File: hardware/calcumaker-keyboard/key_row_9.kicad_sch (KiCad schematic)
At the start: 30 parts, among them SW1 MX, SW10 MX, SW2 MX, SW3 MX, SW4 MX, SW5 MX, SW6 MX, SW7 MX, SW8 MX, SW9 MX

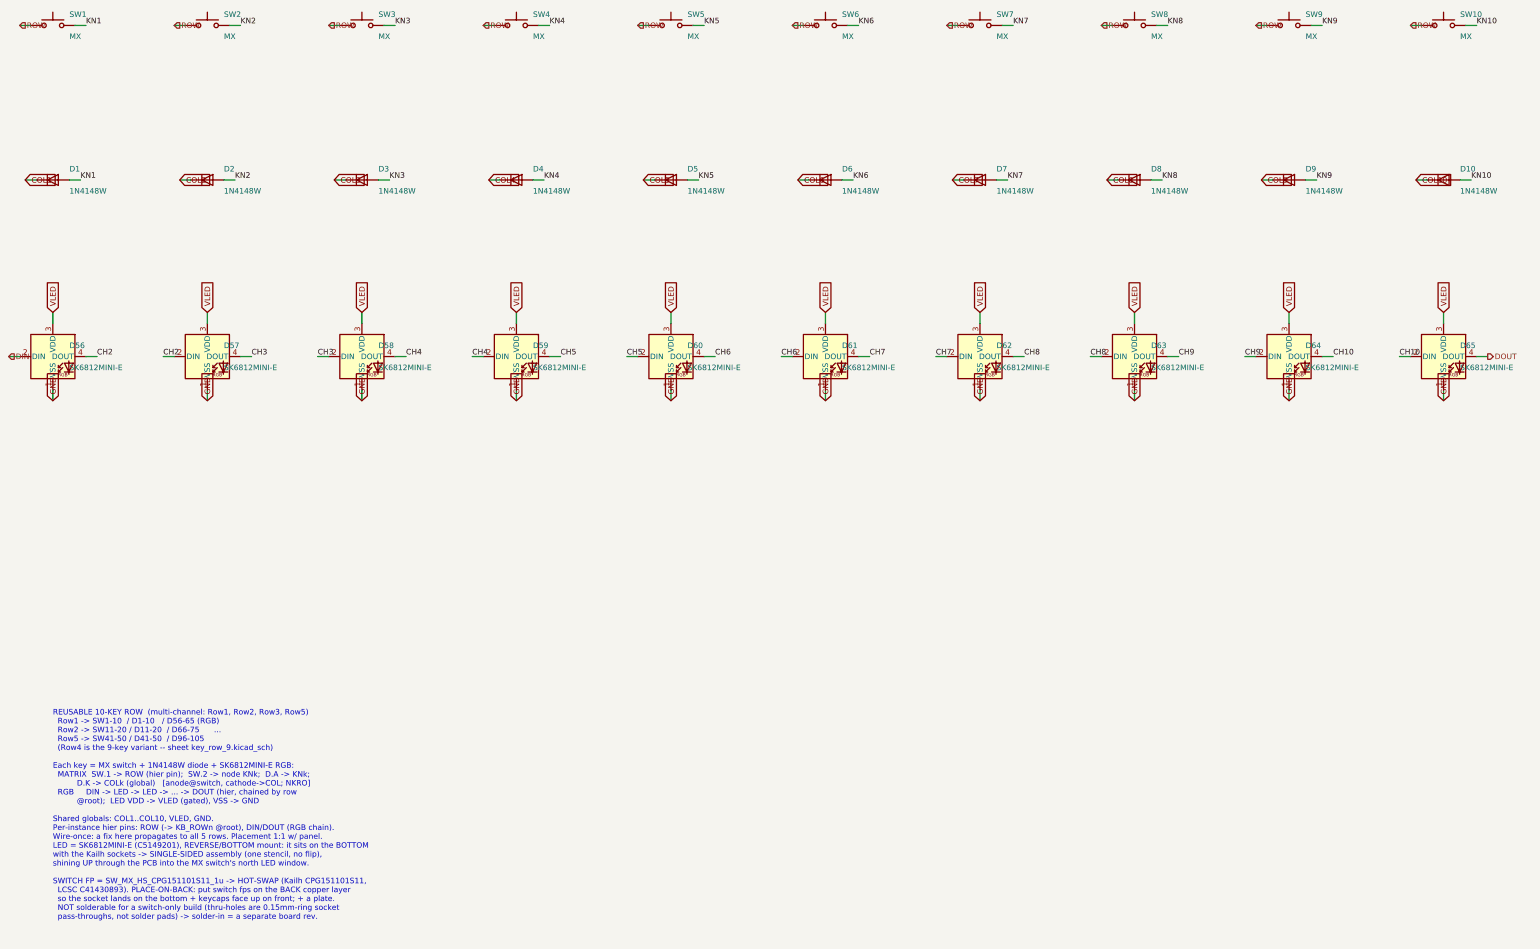
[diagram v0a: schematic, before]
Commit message: hw: regenerate keyboard for the 2U ENTER + vendor the 2U hot-swap footprint
Board files now reflect the 2U ENTER (49 keys):
- key_row.kicad_sch      -> 4 instances (Row1/2/3/5), 30 symbols
- key_row_9.kicad_sch    -> NEW, 1 instance (Row4), 27 symbols: no switch, diode
                            or RGB LED at COL6; refs keep a hole (no SW36/D36/D91)
- root note + rgb_power note updated (49 LEDs, Row4 has 9)

check-calcumaker-keyboard: 176 components (3 fewer), 176/176 footprints assigned,
no duplicate refs, structure sound. Regeneration verified safe first by running the
generator against a scratch copy: the one-off sheets (annunc/kbd_mcu/main_if)
rebuild byte-identical modulo uuids, i.e. nothing was hand-wired.

Vendored calcumaker:SW_MX_HS_CPG151101S11_2u_Vertical -- the 1u hot-swap footprint
plus the four PCB-mount 2U stabilizer NPTH holes (y = +/-11.90mm = 23.8mm spacing;
each wing a 3.05mm hole at x=-7.00 and a 4.00mm at x=+8.24), taken from stock
Button_Switch_Keyboard:SW_Cherry_MX_2.00u_Vertical_PCB and re-expressed about our
origin (already the switch centre). Courtyard grown; 2U keycap envelope on F.Fab.
KiCad 10 parses/plots it (kicad-cli fp export svg).

It is UNUSED by default: we use PLATE-mount stabilizers, which clip into the
switch plate the hot-swap sockets already require, so the PCB needs no stab holes
and ENTER just reuses MX_FP (verified: KiCad's SW_Cherry_MX_2.00u_Vertical_Plate
has the same pad/hole set as the 1u plate fp). PCB-mount would additionally force
a Row5 variant sheet, since ENTER's switch is on the shared 10-key sheet.

Place-on-back is safe: mirroring X maps the stab-hole set onto itself rotated 180,
and a 2U key is symmetric.

Co-Authored-By: Claude Opus 4.8 (1M context) <noreply@anthropic.com>
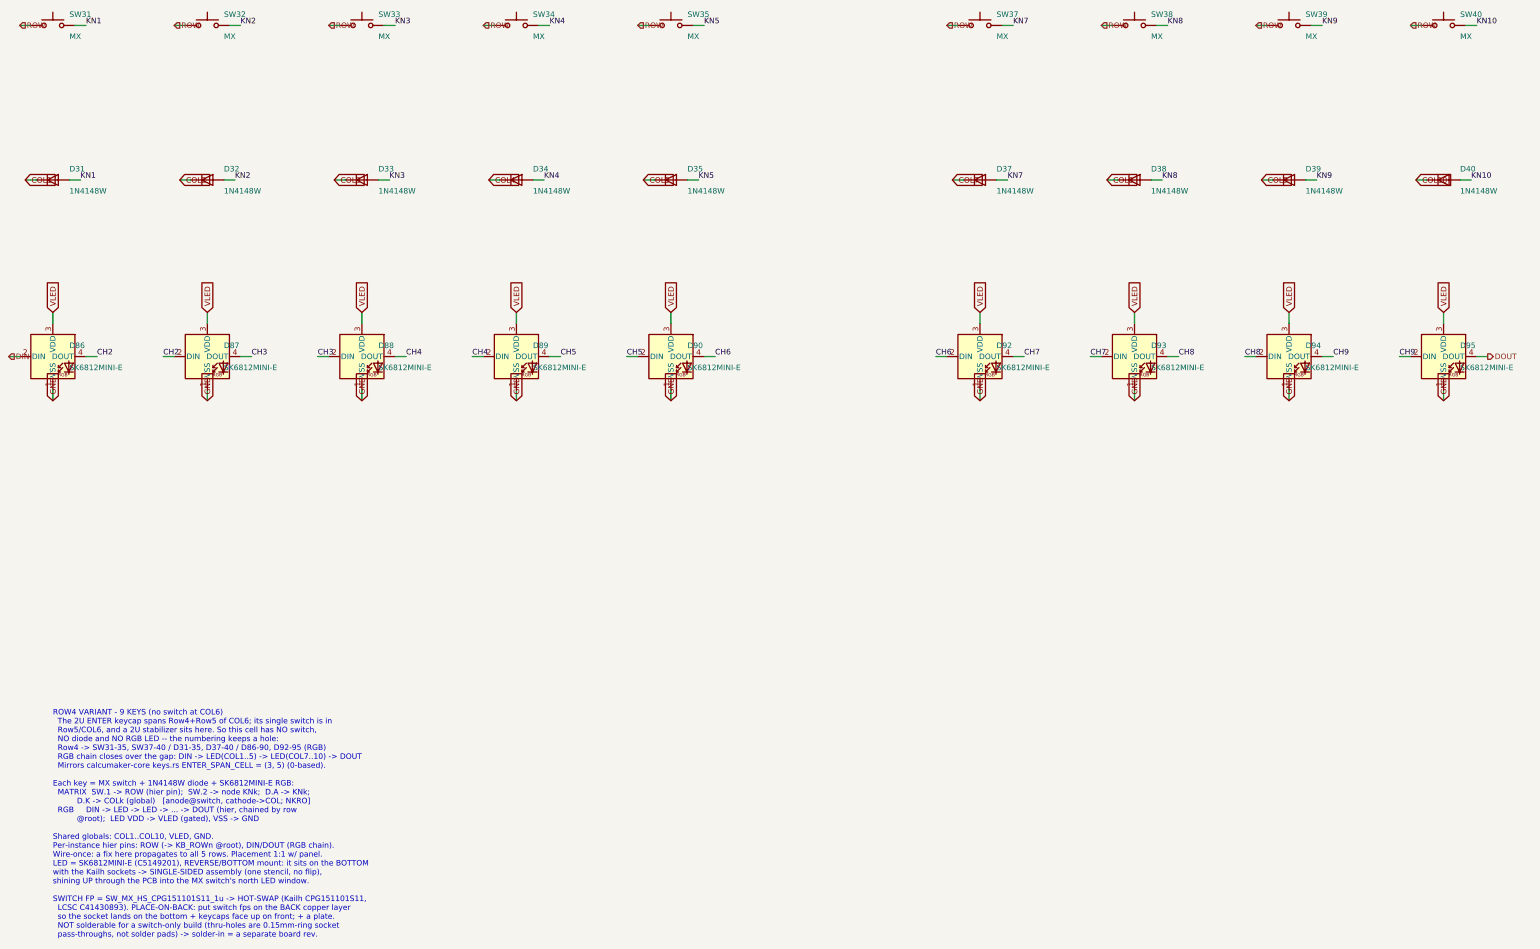
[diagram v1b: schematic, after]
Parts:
- removed D1, D10, D2, D3, D4, D5, D6, D7, D8, D9: 1N4148W, Diode_SMD:D_SOD-123, symbol Device:D
- removed D56, D57, D58, D59, D60, D61, D62, D63, D64, D65: SK6812MINI-E, LED_SMD:LED_SK6812MINI-E_3.2x2.8mm_P1.5mm_ReverseMount, symbol LED:SK6812
- removed SW1, SW10, SW2, SW3, SW4, SW5, SW6, SW7, SW8, SW9: MX, calcumaker:SW_MX_HS_CPG151101S11_1u, symbol Switch:SW_Push
- added D31, D32, D33, D34, D35, D37, D38, D39, D40: 1N4148W, Diode_SMD:D_SOD-123, symbol Device:D
- added D86, D87, D88, D89, D90, D92, D93, D94, D95: SK6812MINI-E, LED_SMD:LED_SK6812MINI-E_3.2x2.8mm_P1.5mm_ReverseMount, symbol LED:SK6812
- added SW31, SW32, SW33, SW34, SW35, SW37, SW38, SW39, SW40: MX, calcumaker:SW_MX_HS_CPG151101S11_1u, symbol Switch:SW_Push
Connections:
- net CH2: now also D86.4 (DOUT), D87.2 (DIN)
- net CH3: now also D87.4 (DOUT), D88.2 (DIN)
- net CH4: now also D88.4 (DOUT), D89.2 (DIN)
- net CH5: now also D89.4 (DOUT), D90.2 (DIN)
- net CH6: now also D90.4 (DOUT), D92.2 (DIN)
- net CH7: now also D92.4 (DOUT), D93.2 (DIN)
- net CH8: now also D93.4 (DOUT), D94.2 (DIN)
- net CH9: now also D94.4 (DOUT), D95.2 (DIN)
- net COL1: now also D31.1 (K)
- net COL10: now also D40.1 (K)
- net COL2: now also D32.1 (K)
- net COL3: now also D33.1 (K)
- net COL4: now also D34.1 (K)
- net COL5: now also D35.1 (K)
- net COL7: now also D37.1 (K)
- net COL8: now also D38.1 (K)
- net COL9: now also D39.1 (K)
- net DIN: now also D86.2 (DIN)
- net DOUT: now also D95.4 (DOUT)
- net GND: now also D86.1 (VSS), D87.1 (VSS), D88.1 (VSS), D89.1 (VSS), D90.1 (VSS), D92.1 (VSS), D93.1 (VSS), D94.1 (VSS), D95.1 (VSS)
- net KN1: now also D31.2 (A), SW31.2
- net KN10: now also D40.2 (A), SW40.2
- net KN2: now also D32.2 (A), SW32.2
- net KN3: now also D33.2 (A), SW33.2
- net KN4: now also D34.2 (A), SW34.2
- net KN5: now also D35.2 (A), SW35.2
- net KN7: now also D37.2 (A), SW37.2
- net KN8: now also D38.2 (A), SW38.2
- net KN9: now also D39.2 (A), SW39.2
- net ROW: now also SW31.1, SW32.1, SW33.1, SW34.1, SW35.1, SW37.1, SW38.1, SW39.1, SW40.1
- net VLED: now also D86.3 (VDD), D87.3 (VDD), D88.3 (VDD), D89.3 (VDD), D90.3 (VDD), D92.3 (VDD), D93.3 (VDD), D94.3 (VDD), D95.3 (VDD)
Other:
- note added: "ROW4 VARIANT - 9 KEYS (no switch at COL6) The 2U ENTER keycap spans Row4+Row5 of COL6; its single switch is in Row5/COL6, and a 2U stabilizer sits here. So this cell has NO switch, NO diode and NO RGB LED -- the numbering keeps a hole: Row4 -> SW31-35, SW37-40 / D31-35, D37-40 / D86-90, D92-95 (RGB) RGB chain closes over the gap: DIN -> LED(COL1..5) -> LED(COL7..10) -> DOUT Mirrors calcumaker-cor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"
- note removed: "REUSABLE 10-KEY ROW (multi-channel: Row1, Row2, Row3, Row5) Row1 -> SW1-10 / D1-10 / D56-65 (RGB) Row2 -> SW11-20 / D11-20 / D66-75 ... Row5 -> SW41-50 / D41-50 / D96-105 (Row4 is the 9-key variant -- sheet key_row_9.kicad_sch) Each key = MX switch + 1N4148W diode + SK6812MINI-E RGB: MATRIX SW.1 -> ROW (hier pin); SW.2 -> node KNk; D.A -> KNk; D.K -> COLk (global) [anode@switch, cathode->COL; NKR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"
- title: Calcumaker 16 — Keyboard — Reusable 10-key row (MX + diode + SK6812MINI-E RGB) -> Calcumaker 16 — Keyboard — Row4 variant: 9 keys (2U ENTER spans COL6 - no switch there)
